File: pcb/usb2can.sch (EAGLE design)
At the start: 35 parts, among them CON1 USB_A_MALESMD, IC1 ADM3053M, IC2 LD117AS33TR, K2 61900419521

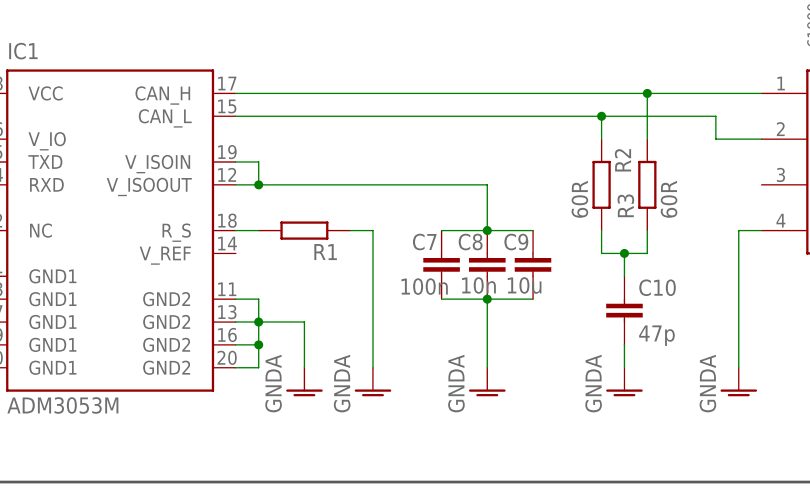
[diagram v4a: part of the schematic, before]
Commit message: pcb: fix capacitor values for ADM3053
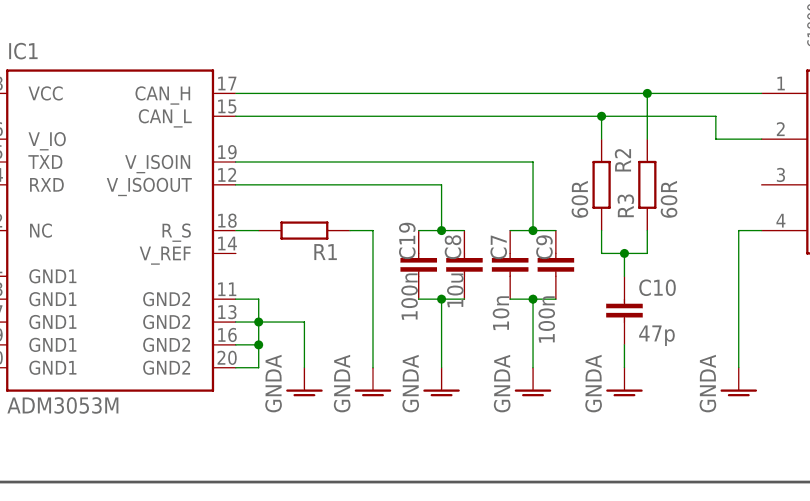
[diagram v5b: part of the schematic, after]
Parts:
- added C19: 100n, rcl:C-EUC0805K
- C7: value 100n -> 10n; device rcl:C-EUC0603K -> rcl:C-EUC0805K
- C8: value 10n -> 10u; device rcl:C-EUC0603K -> rcl:C-EUC0805K
- C9: value 10u -> 100n
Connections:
- removed net VISO: C7.1, C8.1, C9.1, IC1.V_ISOIN, IC1.V_ISOOUT
- new net N$10: C7.1, C9.1, IC1.V_ISOIN
- new net N$8: C19.1, C8.1, IC1.V_ISOOUT
- net GNDA: now also C19.2
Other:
- moved on the sheet: C7, C8, C9
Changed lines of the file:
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@@
 <part name="R1" library="rcl" deviceset="R-EU_" device="R0603"/>
 <part name="GND7" library="supply1" deviceset="GNDA" device=""/>
-<part name="C7" library="rcl" deviceset="C-EU" device="C0603K" value="100n"/>
-<part name="C8" library="rcl" deviceset="C-EU" device="C0603K" value="10n"/>
 <part name="GND8" library="supply1" deviceset="GNDA" device=""/>
-<part name="C9" library="rcl" deviceset="C-EU" device="C0805K" value="10u"/>
+<part name="C9" library="rcl" deviceset="C-EU" device="C0805K" value="100n"/>
 <part name="U$1" library="stm32" deviceset="STM32F072C" device="T"/>
 <part name="K2" library="Wuerth_Elektronik_eiCan_Wire_to_Board_Connectors" deviceset="61900419521" device=""/>
@@
 <part name="GND18" library="supply1" deviceset="GND" device=""/>
 <part name="CON1" library="micro_switch" deviceset="USB_A_MALE" device="SMD"/>
+<part name="C7" library="rcl" deviceset="C-EU" device="C0805K" value="10n"/>
+<part name="C8" library="rcl" deviceset="C-EU" device="C0805K" value="10u"/>
+<part name="C19" library="rcl" deviceset="C-EU" device="C0805K" value="100n"/>
+<part name="GND19" library="supply1" deviceset="GNDA" device=""/>
 </parts>
 <sheets>
@@
 <instance part="R1" gate="G$1" x="127" y="7.62" rot="R180"/>
 <instance part="GND7" gate="1" x="134.62" y="-10.16"/>
-<instance part="C7" gate="G$1" x="142.24" y="5.08" smashed="yes">
-<attribute name="NAME" x="138.938" y="5.461" size="1.778" layer="95"/>
-<attribute name="VALUE" x="137.541" y="0.508" size="1.778" layer="96"/>
-</instance>
-<instance part="C8" gate="G$1" x="147.32" y="5.08" smashed="yes">
-<attribute name="NAME" x="144.018" y="5.461" size="1.778" layer="95"/>
-<attribute name="VALUE" x="144.272" y="0.635" size="1.778" layer="96"/>
-</instance>
-<instance part="GND8" gate="1" x="147.32" y="-10.16"/>
-<instance part="C9" gate="G$1" x="152.4" y="5.08" smashed="yes">
-<attribute name="NAME" x="149.098" y="5.461" size="1.778" layer="95"/>
-<attribute name="VALUE" x="149.352" y="0.635" size="1.778" layer="96"/>
+<instance part="GND8" gate="1" x="142.24" y="-10.16"/>
+<instance part="C9" gate="G$1" x="154.94" y="5.08" smashed="yes">
+<attribute name="NAME" x="154.559" y="4.318" size="1.778" layer="95" rot="R90"/>
+<attribute name="VALUE" x="153.035" y="0.508" size="1.778" layer="96" rot="R270"/>
 </instance>
 <instance part="U$1" gate="G$1" x="25.4" y="162.56"/>
@@
 <instance part="GND18" gate="1" x="-22.86" y="157.48"/>
 <instance part="CON1" gate="G$1" x="-66.04" y="78.74"/>
+<instance part="C7" gate="G$1" x="149.86" y="5.08" smashed="yes">
+<attribute name="NAME" x="149.479" y="4.318" size="1.778" layer="95" rot="R90"/>
+<attribute name="VALUE" x="147.955" y="0.508" size="1.778" layer="96" rot="R270"/>
+</instance>
+<instance part="C8" gate="G$1" x="144.78" y="5.08" smashed="yes">
+<attribute name="NAME" x="144.399" y="4.318" size="1.778" layer="95" rot="R90"/>
+<attribute name="VALUE" x="142.875" y="3.048" size="1.778" layer="96" rot="R270"/>
+</instance>
+<instance part="C19" gate="G$1" x="139.7" y="5.08" smashed="yes">
+<attribute name="NAME" x="139.319" y="4.318" size="1.778" layer="95" rot="R90"/>
+<attribute name="VALUE" x="137.795" y="3.048" size="1.778" layer="96" rot="R270"/>
+</instance>
+<instance part="GND19" gate="1" x="152.4" y="-10.16"/>
 </instances>
 <busses>
@@
 </segment>
 <segment>
-<pinref part="C7" gate="G$1" pin="2"/>
-<pinref part="C8" gate="G$1" pin="2"/>
-<wire x1="147.32" y1="0" x2="142.24" y2="0" width="0.1524" layer="91"/>
-<pinref part="C9" gate="G$1" pin="2"/>
-<wire x1="147.32" y1="0" x2="152.4" y2="0" width="0.1524" layer="91"/>
-<junction x="147.32" y="0"/>
-<pinref part="GND8" gate="1" pin="GNDA"/>
-<wire x1="147.32" y1="-7.62" x2="147.32" y2="0" width="0.1524" layer="91"/>
-</segment>
-<segment>
 <pinref part="C10" gate="G$1" pin="2"/>
 <pinref part="GND10" gate="1" pin="GNDA"/>
@@
 <wire x1="175.26" y1="7.62" x2="175.26" y2="-7.62" width="0.1524" layer="91"/>
 </segment>
+<segment>
+<pinref part="C19" gate="G$1" pin="2"/>
+<pinref part="C8" gate="G$1" pin="2"/>
+<wire x1="139.7" y1="0" x2="142.24" y2="0" width="0.1524" layer="91"/>
+<pinref part="GND8" gate="1" pin="GNDA"/>
+<wire x1="142.24" y1="0" x2="144.78" y2="0" width="0.1524" layer="91"/>
+<wire x1="142.24" y1="0" x2="142.24" y2="-7.62" width="0.1524" layer="91"/>
+<junction x="142.24" y="0"/>
+</segment>
+<segment>
+<pinref part="C9" gate="G$1" pin="2"/>
+<pinref part="C7" gate="G$1" pin="2"/>
+<wire x1="154.94" y1="0" x2="152.4" y2="0" width="0.1524" layer="91"/>
+<pinref part="GND19" gate="1" pin="GNDA"/>
+<wire x1="152.4" y1="0" x2="149.86" y2="0" width="0.1524" layer="91"/>
+<wire x1="152.4" y1="0" x2="152.4" y2="-7.62" width="0.1524" layer="91"/>
+<junction x="152.4" y="0"/>
+</segment>
 </net>
 <net name="N$1" class="0">
@@
 <pinref part="R1" gate="G$1" pin="2"/>
 <wire x1="119.38" y1="7.62" x2="121.92" y2="7.62" width="0.1524" layer="91"/>
-</segment>
-</net>
-<net name="VISO" class="0">
-<segment>
-<pinref part="IC1" gate="G$1" pin="V_ISOIN"/>
-<wire x1="119.38" y1="15.24" x2="121.92" y2="15.24" width="0.1524" layer="91"/>
-<wire x1="121.92" y1="15.24" x2="121.92" y2="12.7" width="0.1524" layer="91"/>
-<pinref part="IC1" gate="G$1" pin="V_ISOOUT"/>
-<wire x1="121.92" y1="12.7" x2="119.38" y2="12.7" width="0.1524" layer="91"/>
-<wire x1="121.92" y1="12.7" x2="147.32" y2="12.7" width="0.1524" layer="91"/>
-<junction x="121.92" y="12.7"/>
-<pinref part="C9" gate="G$1" pin="1"/>
-<pinref part="C8" gate="G$1" pin="1"/>
-<wire x1="147.32" y1="7.62" x2="152.4" y2="7.62" width="0.1524" layer="91"/>
-<junction x="147.32" y="7.62"/>
-<pinref part="C7" gate="G$1" pin="1"/>
-<wire x1="142.24" y1="7.62" x2="147.32" y2="7.62" width="0.1524" layer="91"/>
-<wire x1="147.32" y1="12.7" x2="147.32" y2="7.62" width="0.1524" layer="91"/>
 </segment>
 </net>
@@
 </segment>
 </net>
+<net name="N$8" class="0">
+<segment>
+<pinref part="C19" gate="G$1" pin="1"/>
+<pinref part="C8" gate="G$1" pin="1"/>
+<wire x1="139.7" y1="7.62" x2="142.24" y2="7.62" width="0.1524" layer="91"/>
+<wire x1="142.24" y1="7.62" x2="144.78" y2="7.62" width="0.1524" layer="91"/>
+<wire x1="142.24" y1="7.62" x2="142.24" y2="12.7" width="0.1524" layer="91"/>
+<junction x="142.24" y="7.62"/>
+<pinref part="IC1" gate="G$1" pin="V_ISOOUT"/>
+<wire x1="142.24" y1="12.7" x2="119.38" y2="12.7" width="0.1524" layer="91"/>
+</segment>
+</net>
+<net name="N$10" class="0">
+<segment>
+<pinref part="C7" gate="G$1" pin="1"/>
+<pinref part="C9" gate="G$1" pin="1"/>
+<wire x1="149.86" y1="7.62" x2="152.4" y2="7.62" width="0.1524" layer="91"/>
+<wire x1="152.4" y1="7.62" x2="154.94" y2="7.62" width="0.1524" layer="91"/>
+<wire x1="152.4" y1="7.62" x2="152.4" y2="15.24" width="0.1524" layer="91"/>
+<junction x="152.4" y="7.62"/>
+<pinref part="IC1" gate="G$1" pin="V_ISOIN"/>
+<wire x1="152.4" y1="15.24" x2="119.38" y2="15.24" width="0.1524" layer="91"/>
+</segment>
+</net>

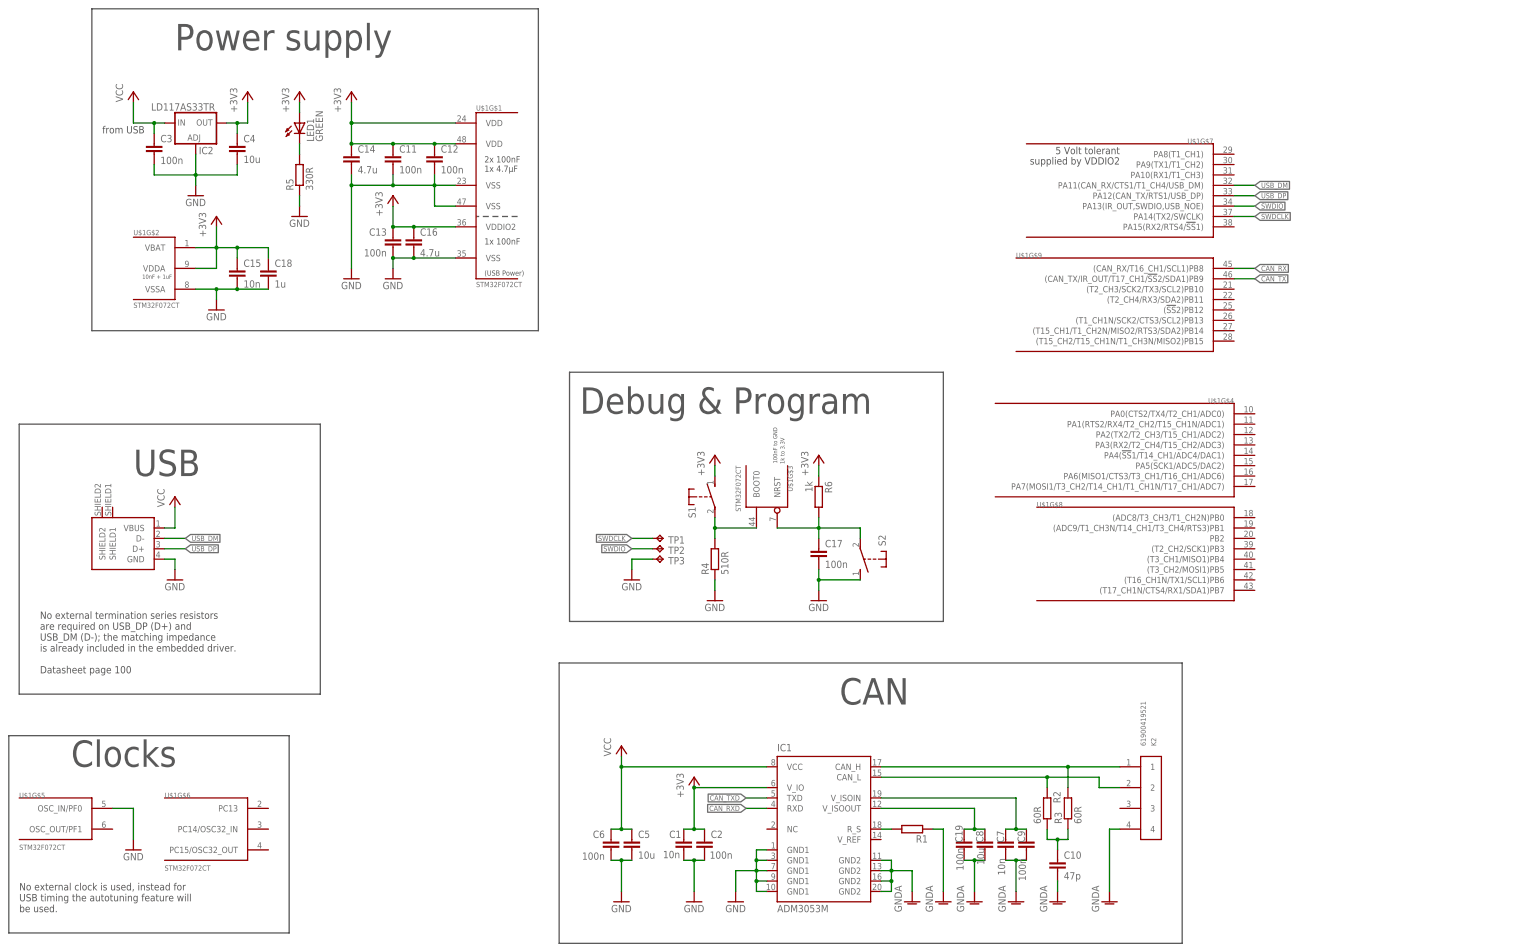
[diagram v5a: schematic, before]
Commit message: pcb: final routing and small schamtic fixes
 * Testpad for UART TX
 * 4 User LEDs
 * 1 User Button
 * RCA CAN-connector
 * Bypass capacitor for BOOT0
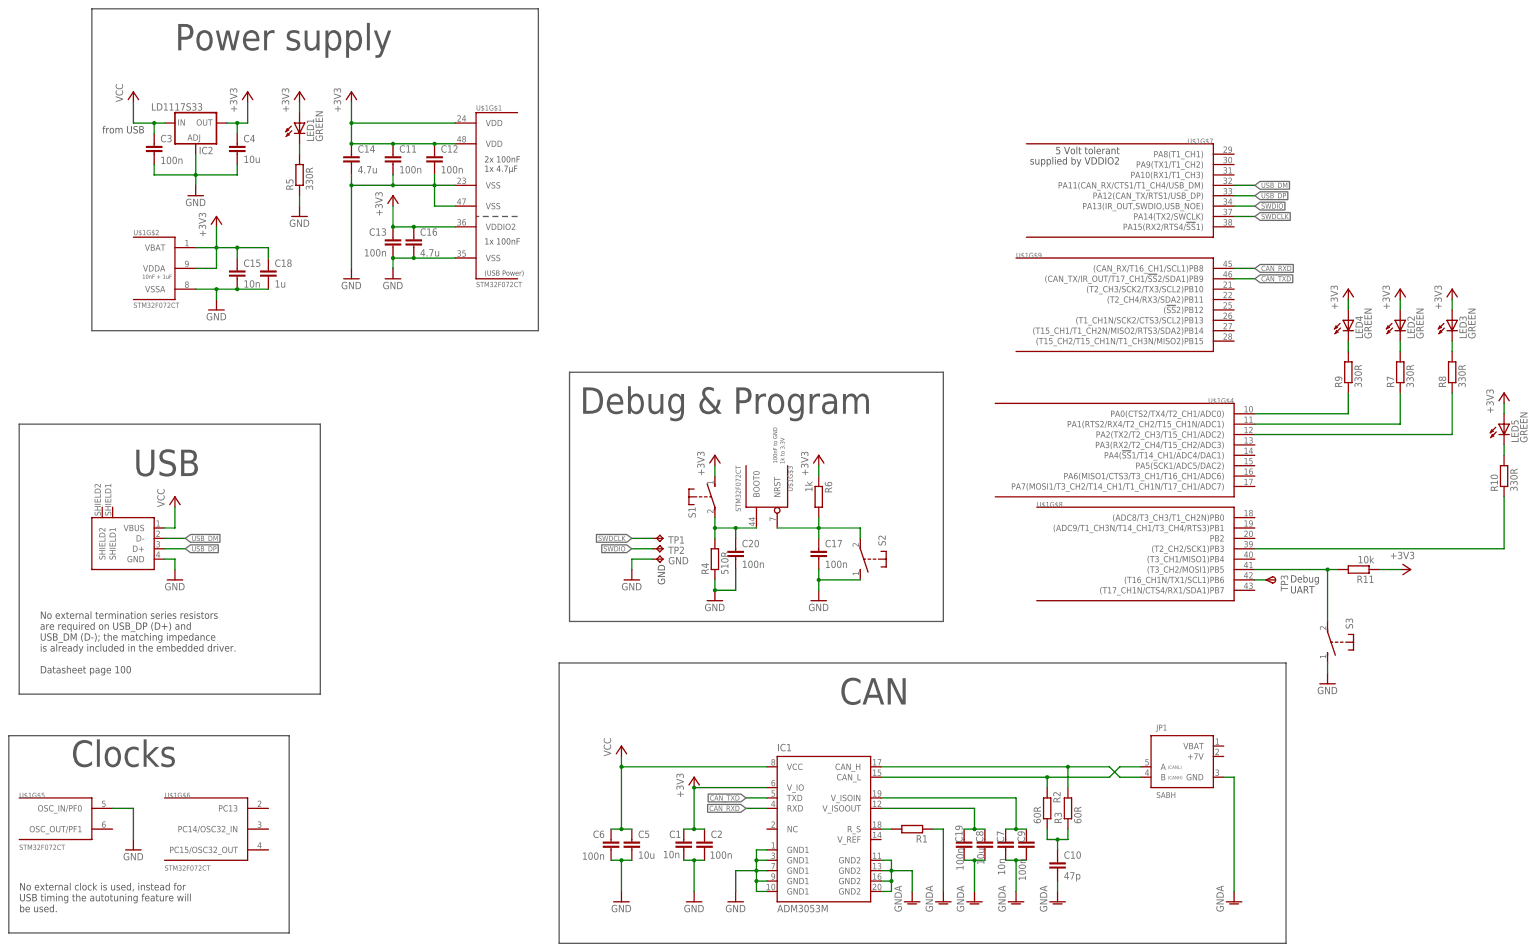
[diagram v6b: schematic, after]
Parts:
- removed K2: 61900419521, Wuerth_Elektronik_eiCan_Wire_to_Board_Connectors:61900419521
- added C20: 100n, rcl:C-EUC0603
- added GND: TPB2,54, testpad:TPB2,54
- added JP1: SABH, rca_stecker:SABH
- added LED2, LED3, LED4, LED5: GREEN, led:LEDCHIPLED_0603
- added R10, R7, R8, R9: 330R, resistor:R-EU_R0603
- added R11: 10k, resistor:R-EU_R0603
- added S3: MICRO_SWITCH_3X6X2.5S, micro_switch:MICRO_SWITCH_3X6X2.5S
- IC2: value LD117AS33TR -> LD1117S33
- TP3: value TPB2,54 -> TPSTP07R; device testpad:TPB2,54 -> testpad:TPSTP07R
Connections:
- removed net CAN_RX: U$1G$9.(CAN_RX/T16_CH1/SCL1)PB8
- removed net CAN_TX: U$1G$9.(CAN_TX/IR_OUT/T17_CH1/!SS!2/SDA1)PB9
- new net N$11: R11.2, S3.2, U$1G$8.(T3_CH2/MOSI1)PB5
- new net N$12: LED3.C, R8.2
- new net N$13: LED4.C, R9.2
- new net N$14: R9.1, U$1G$4.PA0(CTS2/TX4/T2_CH1/ADC0)
- new net N$15: R7.1, U$1G$4.PA1(RTS2/RX4/T2_CH2/T15_CH1N/ADC1)
- new net N$16: R8.1, U$1G$4.PA2(TX2/T2_CH3/T15_CH1/ADC2)
- new net N$17: LED5.C, R10.2
- new net N$18: R10.1, U$1G$8.(T2_CH2/SCK1)PB3
- new net N$9: LED2.C, R7.2
- new net TX: TP3.PP, U$1G$8.(T16_CH1N/TX1/SCL1)PB6
- net +3V3: now also LED2.A, LED3.A, LED4.A, LED5.A, R11.1
- net CAN_RXD: now also U$1G$9.(CAN_RX/T16_CH1/SCL1)PB8
- net CAN_TXD: now also U$1G$9.(CAN_TX/IR_OUT/T17_CH1/!SS!2/SDA1)PB9
- net GND: now also C20.2, GND.TP, S3.1; no longer TP3.TP
- net GNDA: now also JP1.GND; no longer K2.4
- net N$2: now also JP1.A; no longer K2.2
- net N$3: now also JP1.B; no longer K2.1
- net N$6: now also C20.1
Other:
- note added: "Debug UART"
